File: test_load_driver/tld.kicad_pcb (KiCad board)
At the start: 2 copper layers, 6 parts, among them J1 input, J2 power, J3 output, Q1 IRFZ44N, U1 TC427

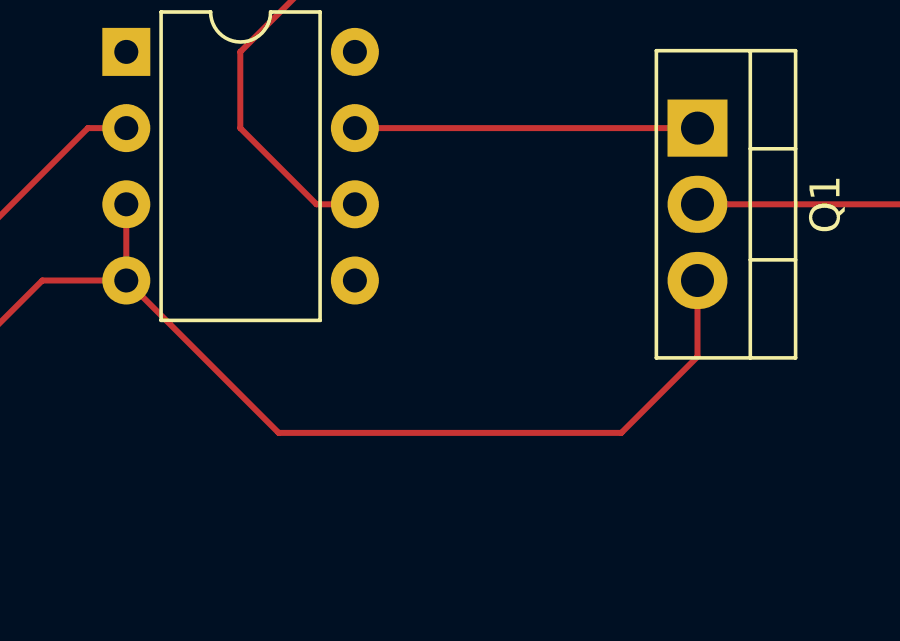
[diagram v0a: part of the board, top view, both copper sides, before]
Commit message: added debouncing capacitor
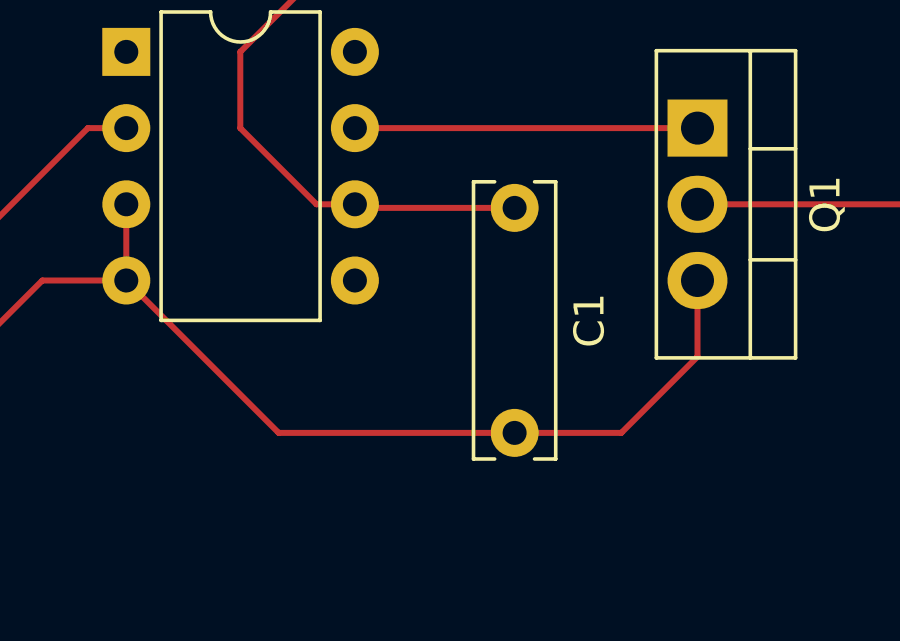
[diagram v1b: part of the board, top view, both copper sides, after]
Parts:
- added C1: 100nF, Capacitor_THT:C_Rect_L9.0mm_W2.5mm_P7.50mm_MKT, F.Cu at (120.9, 58.5)
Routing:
- net Net-(J3-Pin_1): track 59.4 -> 64.8 mm
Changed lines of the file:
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@@
+    )
+  )
+  (footprint "Capacitor_THT:C_Rect_L9.0mm_W2.5mm_P7.50mm_MKT" (layer "F.Cu")
+    (at 120.904 58.54 -90)
+    (descr "C, Rect series, Radial, pin pitch=7.50mm, , length*width=9*2.5mm^2, Capacitor, https://en.tdk.eu/inf/20/20/db/fc_2009/MKT_B32560_564.pdf")
+    (tags "C Rect series Radial pin pitch 7.50mm  length 9mm width 2.5mm Capacitor")
+    (property "Sheetfile" "tld.kicad_sch")
+    (property "Sheetname" "")
+    (property "ki_description" "Unpolarized capacitor")
+    (property "ki_keywords" "cap capacitor")
+    (attr through_hole)
+    (fp_text reference "C1" (at 3.75 -2.5 90) (layer "F.SilkS")
+        (effects (font (size 1 1) (thickness 0.15)))
+    )
+    (fp_text value "100nF" (at 3.75 2.5 90) (layer "F.Fab")
+        (effects (font (size 1 1) (thickness 0.15)))
+    )
+    (fp_text user "${REFERENCE}" (at 3.75 0 90) (layer "F.Fab")
+        (effects (font (size 1 1) (thickness 0.15)))
+    )
+    (fp_line (start -0.87 -1.37) (end -0.87 -0.665)
+      (stroke (width 0.12) (type solid)) (layer "F.SilkS"))
+    (fp_line (start -0.87 -1.37) (end 8.37 -1.37)
+      (stroke (width 0.12) (type solid)) (layer "F.SilkS"))
+    (fp_line (start -0.87 0.665) (end -0.87 1.37)
+      (stroke (width 0.12) (type solid)) (layer "F.SilkS"))
+    (fp_line (start -0.87 1.37) (end 8.37 1.37)
+      (stroke (width 0.12) (type solid)) (layer "F.SilkS"))
+    (fp_line (start 8.37 -1.37) (end 8.37 -0.665)
+      (stroke (width 0.12) (type solid)) (layer "F.SilkS"))
+    (fp_line (start 8.37 0.665) (end 8.37 1.37)
+      (stroke (width 0.12) (type solid)) (layer "F.SilkS"))
+    (fp_line (start -1.05 -1.5) (end -1.05 1.5)
+      (stroke (width 0.05) (type solid)) (layer "F.CrtYd"))
+    (fp_line (start -1.05 1.5) (end 8.55 1.5)
+      (stroke (width 0.05) (type solid)) (layer "F.CrtYd"))
+    (fp_line (start 8.55 -1.5) (end -1.05 -1.5)
+      (stroke (width 0.05) (type solid)) (layer "F.CrtYd"))
+    (fp_line (start 8.55 1.5) (end 8.55 -1.5)
+      (stroke (width 0.05) (type solid)) (layer "F.CrtYd"))
+    (fp_line (start -0.75 -1.25) (end -0.75 1.25)
+      (stroke (width 0.1) (type solid)) (layer "F.Fab"))
+    (fp_line (start -0.75 1.25) (end 8.25 1.25)
+      (stroke (width 0.1) (type solid)) (layer "F.Fab"))
+    (fp_line (start 8.25 -1.25) (end -0.75 -1.25)
+      (stroke (width 0.1) (type solid)) (layer "F.Fab"))
+    (fp_line (start 8.25 1.25) (end 8.25 -1.25)
+      (stroke (width 0.1) (type solid)) (layer "F.Fab"))
+    (pad "1" thru_hole circle (at 0 0 270) (size 1.6 1.6) (drill 0.8) (layers "*.Cu" "*.Mask")
+      (net 4 "Net-(J3-Pin_1)") (pintype "passive"))
+    (pad "2" thru_hole circle (at 7.5 0 270) (size 1.6 1.6) (drill 0.8) (layers "*.Cu" "*.Mask")
+      (net 3 "GND") (pintype "passive"))
+    (model "${KICAD6_3DMODEL_DIR}/Capacitor_THT.3dshapes/C_Rect_L9.0mm_W2.5mm_P7.50mm_MKT.wrl"
+      (offset (xyz 0 0 0))
+      (scale (xyz 1 1 1))
+      (rotate (xyz 0 0 0))
     )
   )
@@
   (segment (start 105.16 60.96) (end 95.76 70.36) (width 0.2) (layer "F.Cu") (net 3))
   (segment (start 113.04 66.04) (end 107.96 60.96) (width 0.2) (layer "F.Cu") (net 3))
+  (segment (start 120.904 66.04) (end 124.46 66.04) (width 0.2) (layer "F.Cu") (net 3))
   (segment (start 107.96 60.96) (end 105.16 60.96) (width 0.2) (layer "F.Cu") (net 3))
+  (segment (start 113.04 66.04) (end 120.904 66.04) (width 0.2) (layer "F.Cu") (net 3))
   (segment (start 66.04 68.58) (end 66.8 70.36) (width 0.2) (layer "F.Cu") (net 3))
   (segment (start 95.76 70.36) (end 68.58 70.36) (width 0.2) (layer "F.Cu") (net 3))
   (segment (start 68.58 55.88) (end 68.58 60.96) (width 0.2) (layer "F.Cu") (net 3))
   (segment (start 127 63.5) (end 124.46 66.04) (width 0.2) (layer "F.Cu") (net 3))
-  (segment (start 124.46 66.04) (end 113.04 66.04) (width 0.2) (layer "F.Cu") (net 3))
   (segment (start 66.04 63.5) (end 66.04 68.58) (width 0.2) (layer "F.Cu") (net 3))
   (segment (start 127 60.96) (end 127 63.5) (width 0.2) (layer "F.Cu") (net 3))
+  (segment (start 115.7 58.54) (end 115.58 58.42) (width 0.2) (layer "F.Cu") (net 4))
+  (segment (start 120.904 58.54) (end 115.7 58.54) (width 0.2) (layer "F.Cu") (net 4))
   (segment (start 111.76 53.34) (end 116.84 48.26) (width 0.2) (layer "F.Cu") (net 4))
   (segment (start 134.62 48.26) (end 137.16 50.8) (width 0.2) (layer "F.Cu") (net 4))

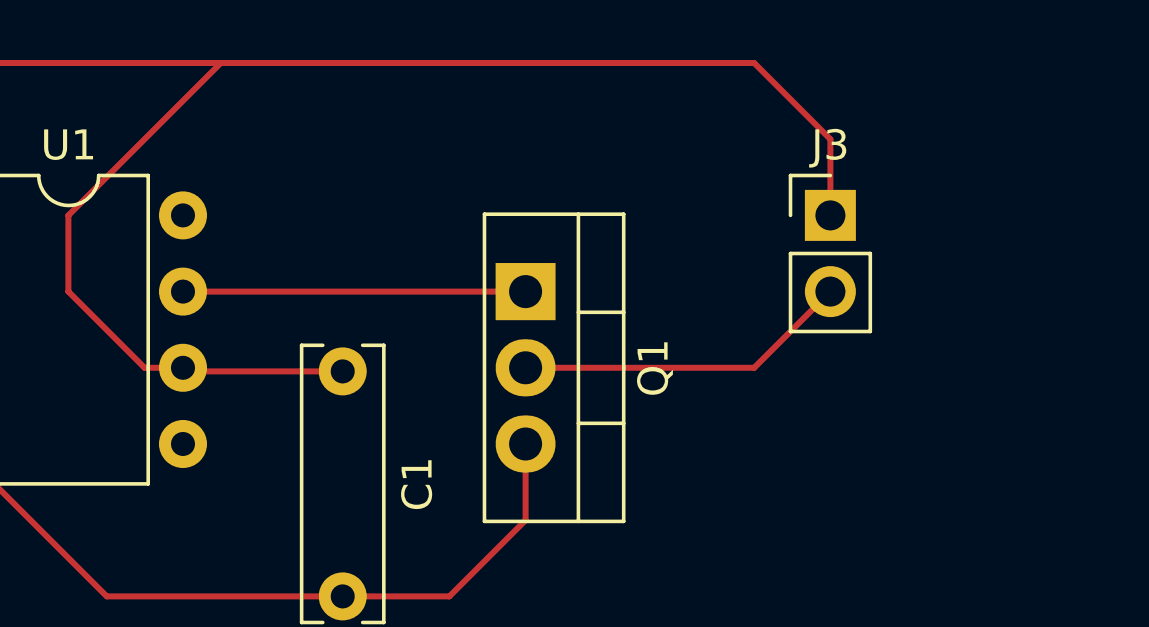
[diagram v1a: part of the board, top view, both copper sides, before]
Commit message: added 1N4001 diode to protect the transistor
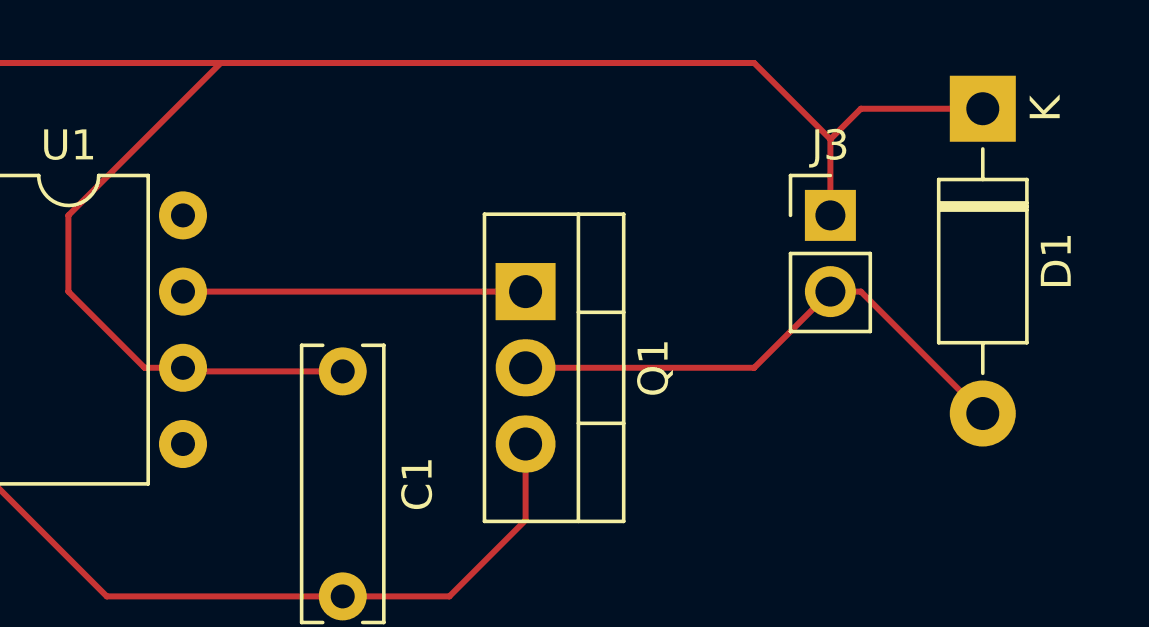
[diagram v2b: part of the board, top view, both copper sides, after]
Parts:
- added D1: 1N4001, Diode_THT:D_DO-41_SOD81_P10.16mm_Horizontal, F.Cu at (142.2, 49.8)
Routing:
- net Net-(D1-A): track 11.2 -> 18.0 mm
- net Net-(D1-K): track 64.8 -> 70.3 mm

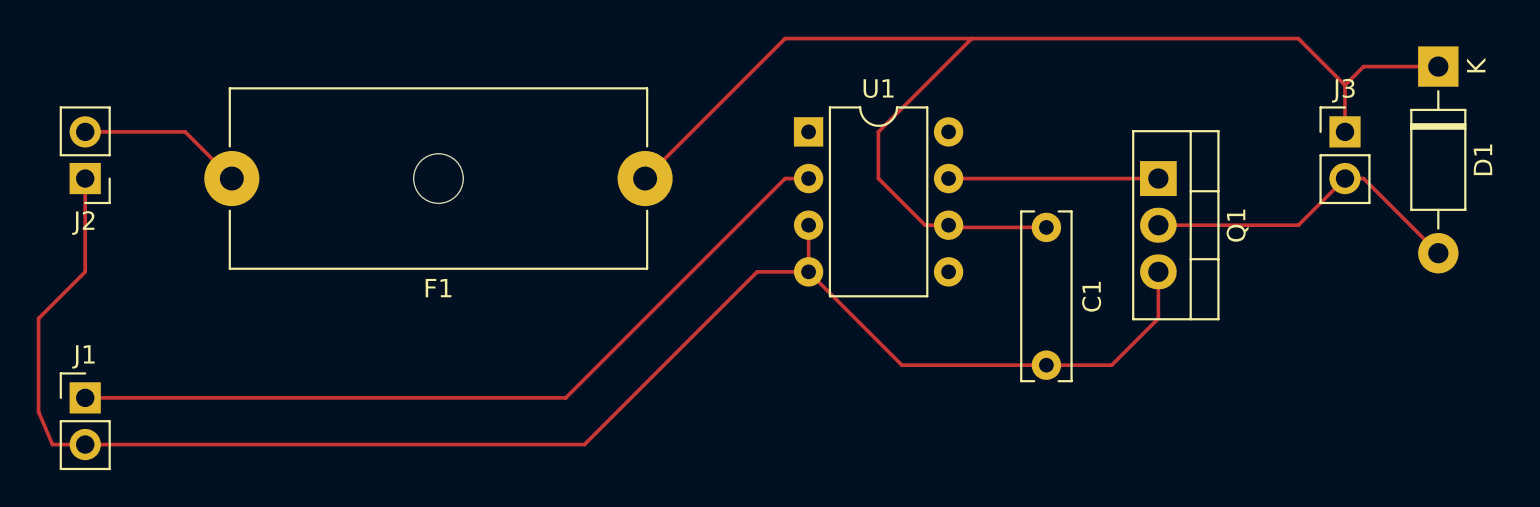
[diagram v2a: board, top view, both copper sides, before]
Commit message: non-inverting version
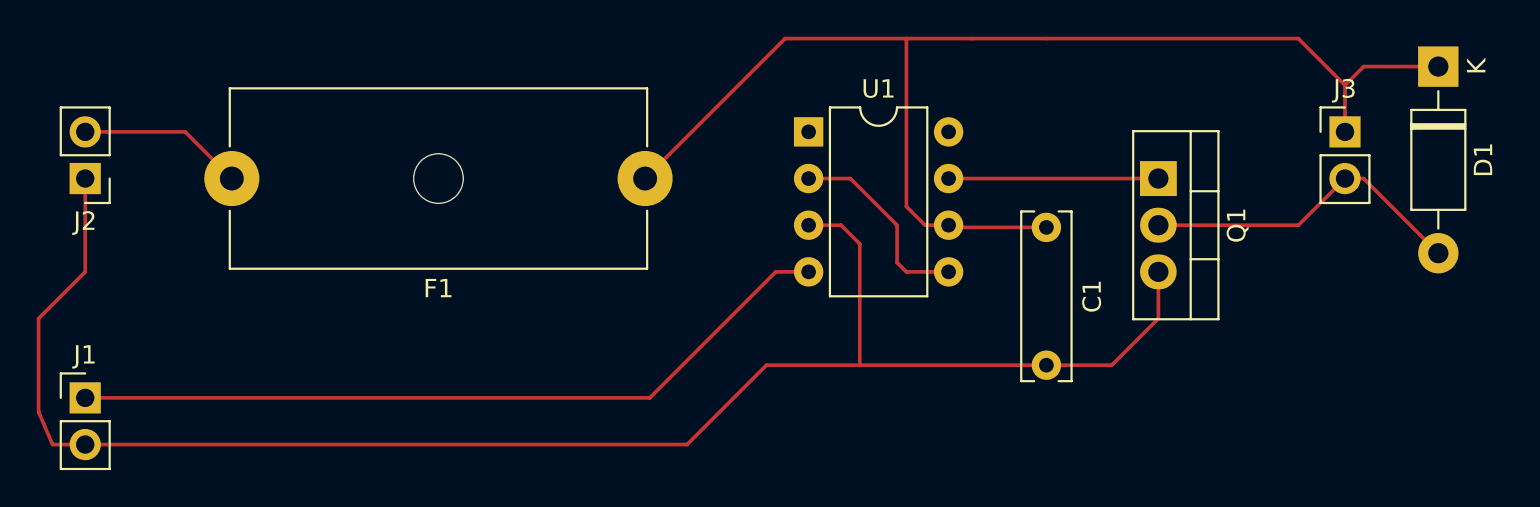
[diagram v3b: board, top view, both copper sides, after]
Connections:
- U1 pad 2: Net-(J1-Pin_1) -> Net-(U1-IN_A)
- U1 pad 4: GND -> Net-(J1-Pin_1)
- U1 pad 5: unconnected-(U1-OUT_B-Pad5) -> Net-(U1-IN_A)
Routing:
- net Net-(U1-IN_A): track 0.00 -> 10.9 mm
- net GND: track 88.0 -> 91.1 mm
- net Net-(D1-K): track 70.3 -> 67.6 mm
- net Net-(J1-Pin_1): track 44.3 -> 42.2 mm
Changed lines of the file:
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@@
   (net 6 "Net-(J1-Pin_1)")
   (net 7 "unconnected-(U1-NC-Pad1)")
-  (net 8 "unconnected-(U1-OUT_B-Pad5)")
-  (net 9 "unconnected-(U1-NC-Pad8)")
+  (net 8 "unconnected-(U1-NC-Pad8)")
+  (net 9 "Net-(U1-IN_A)")
   (footprint "Fuse:Fuseholder_Cylinder-5x20mm_Schurter_0031_8201_Horizontal_Open" (layer "F.Cu")
     (at 99.06 55.88 180)
@@
       (net 7 "unconnected-(U1-NC-Pad1)") (pinfunction "NC") (pintype "no_connect"))
     (pad "2" thru_hole oval (at 0 2.54) (size 1.6 1.6) (drill 0.8) (layers "*.Cu" "*.Mask")
-      (net 6 "Net-(J1-Pin_1)") (pinfunction "IN_A") (pintype "input"))
+      (net 9 "Net-(U1-IN_A)") (pinfunction "IN_A") (pintype "input"))
     (pad "3" thru_hole oval (at 0 5.08) (size 1.6 1.6) (drill 0.8) (layers "*.Cu" "*.Mask")
       (net 3 "GND") (pinfunction "GND") (pintype "power_in"))
     (pad "4" thru_hole oval (at 0 7.62) (size 1.6 1.6) (drill 0.8) (layers "*.Cu" "*.Mask")
-      (net 3 "GND") (pinfunction "IN_B") (pintype "input"))
+      (net 6 "Net-(J1-Pin_1)") (pinfunction "IN_B") (pintype "input"))
     (pad "5" thru_hole oval (at 7.62 7.62) (size 1.6 1.6) (drill 0.8) (layers "*.Cu" "*.Mask")
-      (net 8 "unconnected-(U1-OUT_B-Pad5)") (pinfunction "OUT_B") (pintype "output"))
+      (net 9 "Net-(U1-IN_A)") (pinfunction "OUT_B") (pintype "output"))
     (pad "6" thru_hole oval (at 7.62 5.08) (size 1.6 1.6) (drill 0.8) (layers "*.Cu" "*.Mask")
       (net 2 "Net-(D1-K)") (pinfunction "V+") (pintype "power_in"))
@@
       (net 1 "Net-(Q1-G)") (pinfunction "OUT_A") (pintype "output"))
     (pad "8" thru_hole oval (at 7.62 0) (size 1.6 1.6) (drill 0.8) (layers "*.Cu" "*.Mask")
-      (net 9 "unconnected-(U1-NC-Pad8)") (pinfunction "NC") (pintype "no_connect"))
+      (net 8 "unconnected-(U1-NC-Pad8)") (pinfunction "NC") (pintype "no_connect"))
     (model "${KICAD6_3DMODEL_DIR}/Package_DIP.3dshapes/DIP-8_W7.62mm.wrl"
       (offset (xyz 0 0 0))
@@
   )
   (segment (start 127 55.88) (end 115.58 55.88) (width 0.2) (layer "F.Cu") (net 1))
+  (segment (start 115.58 58.42) (end 114.3 58.42) (width 0.2) (layer "F.Cu") (net 2))
+  (segment (start 134.62 48.26) (end 137.16 50.8) (width 0.2) (layer "F.Cu") (net 2))
+  (segment (start 120.904 48.26) (end 134.62 48.26) (width 0.2) (layer "F.Cu") (net 2))
+  (segment (start 120.904 58.54) (end 115.7 58.54) (width 0.2) (layer "F.Cu") (net 2))
+  (segment (start 113.284 57.404) (end 113.284 48.26) (width 0.2) (layer "F.Cu") (net 2))
+  (segment (start 106.68 48.26) (end 113.284 48.26) (width 0.2) (layer "F.Cu") (net 2))
+  (segment (start 113.284 48.26) (end 116.84 48.26) (width 0.2) (layer "F.Cu") (net 2))
+  (segment (start 116.84 48.26) (end 120.904 48.26) (width 0.2) (layer "F.Cu") (net 2))
   (segment (start 115.7 58.54) (end 115.58 58.42) (width 0.2) (layer "F.Cu") (net 2))
-  (segment (start 120.904 58.54) (end 115.7 58.54) (width 0.2) (layer "F.Cu") (net 2))
-  (segment (start 111.76 53.34) (end 116.84 48.26) (width 0.2) (layer "F.Cu") (net 2))
-  (segment (start 134.62 48.26) (end 137.16 50.8) (width 0.2) (layer "F.Cu") (net 2))
-  (segment (start 115.58 58.42) (end 114.3 58.42) (width 0.2) (layer "F.Cu") (net 2))
-  (segment (start 114.3 58.42) (end 111.76 55.88) (width 0.2) (layer "F.Cu") (net 2))
-  (segment (start 106.68 48.26) (end 116.84 48.26) (width 0.2) (layer "F.Cu") (net 2))
-  (segment (start 111.76 55.88) (end 111.76 53.34) (width 0.2) (layer "F.Cu") (net 2))
+  (segment (start 114.3 58.42) (end 113.284 57.404) (width 0.2) (layer "F.Cu") (net 2))
   (segment (start 138.176 49.784) (end 137.16 50.8) (width 0.2) (layer "F.Cu") (net 2))
   (segment (start 137.16 50.8) (end 137.16 53.34) (width 0.2) (layer "F.Cu") (net 2))
   (segment (start 99.06 55.88) (end 106.68 48.26) (width 0.2) (layer "F.Cu") (net 2))
   (segment (start 142.24 49.784) (end 138.176 49.784) (width 0.2) (layer "F.Cu") (net 2))
-  (segment (start 116.84 48.26) (end 134.62 48.26) (width 0.2) (layer "F.Cu") (net 2))
-  (segment (start 107.96 60.96) (end 107.96 58.42) (width 0.2) (layer "F.Cu") (net 3))
+  (segment (start 110.744 66.04) (end 105.664 66.04) (width 0.2) (layer "F.Cu") (net 3))
+  (segment (start 107.96 58.42) (end 109.728 58.42) (width 0.2) (layer "F.Cu") (net 3))
+  (segment (start 109.728 58.42) (end 110.744 59.436) (width 0.2) (layer "F.Cu") (net 3))
   (segment (start 66.8 70.36) (end 68.58 70.36) (width 0.2) (layer "F.Cu") (net 3))
   (segment (start 68.58 60.96) (end 66.04 63.5) (width 0.2) (layer "F.Cu") (net 3))
-  (segment (start 105.16 60.96) (end 95.76 70.36) (width 0.2) (layer "F.Cu") (net 3))
-  (segment (start 113.04 66.04) (end 107.96 60.96) (width 0.2) (layer "F.Cu") (net 3))
+  (segment (start 120.904 66.04) (end 110.744 66.04) (width 0.2) (layer "F.Cu") (net 3))
+  (segment (start 110.744 59.436) (end 110.744 66.04) (width 0.2) (layer "F.Cu") (net 3))
   (segment (start 120.904 66.04) (end 124.46 66.04) (width 0.2) (layer "F.Cu") (net 3))
-  (segment (start 107.96 60.96) (end 105.16 60.96) (width 0.2) (layer "F.Cu") (net 3))
-  (segment (start 113.04 66.04) (end 120.904 66.04) (width 0.2) (layer "F.Cu") (net 3))
   (segment (start 66.04 68.58) (end 66.8 70.36) (width 0.2) (layer "F.Cu") (net 3))
-  (segment (start 95.76 70.36) (end 68.58 70.36) (width 0.2) (layer "F.Cu") (net 3))
   (segment (start 68.58 55.88) (end 68.58 60.96) (width 0.2) (layer "F.Cu") (net 3))
   (segment (start 127 63.5) (end 124.46 66.04) (width 0.2) (layer "F.Cu") (net 3))
+  (segment (start 68.58 70.36) (end 101.344 70.36) (width 0.2) (layer "F.Cu") (net 3))
+  (segment (start 101.344 70.36) (end 105.664 66.04) (width 0.2) (layer "F.Cu") (net 3))
   (segment (start 66.04 63.5) (end 66.04 68.58) (width 0.2) (layer "F.Cu") (net 3))
   (segment (start 127 60.96) (end 127 63.5) (width 0.2) (layer "F.Cu") (net 3))
@@
   (segment (start 68.58 53.34) (end 74.02 53.34) (width 0.2) (layer "F.Cu") (net 5))
   (segment (start 74.02 53.34) (end 76.56 55.88) (width 0.2) (layer "F.Cu") (net 5))
-  (segment (start 94.74 67.82) (end 106.68 55.88) (width 0.2) (layer "F.Cu") (net 6))
-  (segment (start 68.58 67.82) (end 94.74 67.82) (width 0.2) (layer "F.Cu") (net 6))
-  (segment (start 106.68 55.88) (end 107.96 55.88) (width 0.2) (layer "F.Cu") (net 6))
+  (segment (start 106.172 60.96) (end 107.96 60.96) (width 0.2) (layer "F.Cu") (net 6))
+  (segment (start 99.312 67.82) (end 106.172 60.96) (width 0.2) (layer "F.Cu") (net 6))
+  (segment (start 68.58 67.82) (end 99.312 67.82) (width 0.2) (layer "F.Cu") (net 6))
+  (segment (start 107.96 55.88) (end 110.236 55.88) (width 0.2) (layer "F.Cu") (net 9))
+  (segment (start 110.236 55.88) (end 112.776 58.42) (width 0.2) (layer "F.Cu") (net 9))
+  (segment (start 112.776 58.42) (end 112.776 60.452) (width 0.2) (layer "F.Cu") (net 9))
+  (segment (start 112.776 60.452) (end 113.284 60.96) (width 0.2) (layer "F.Cu") (net 9))
+  (segment (start 113.284 60.96) (end 115.58 60.96) (width 0.2) (layer "F.Cu") (net 9))
 )
